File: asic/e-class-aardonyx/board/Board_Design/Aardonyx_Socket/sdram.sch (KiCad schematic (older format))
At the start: 30 parts, among them J4 Conn_1x4, U15 SKT32E, U2 IS42S32160F-TSOP2, U3 CDCE913PW, Y2 27MHz

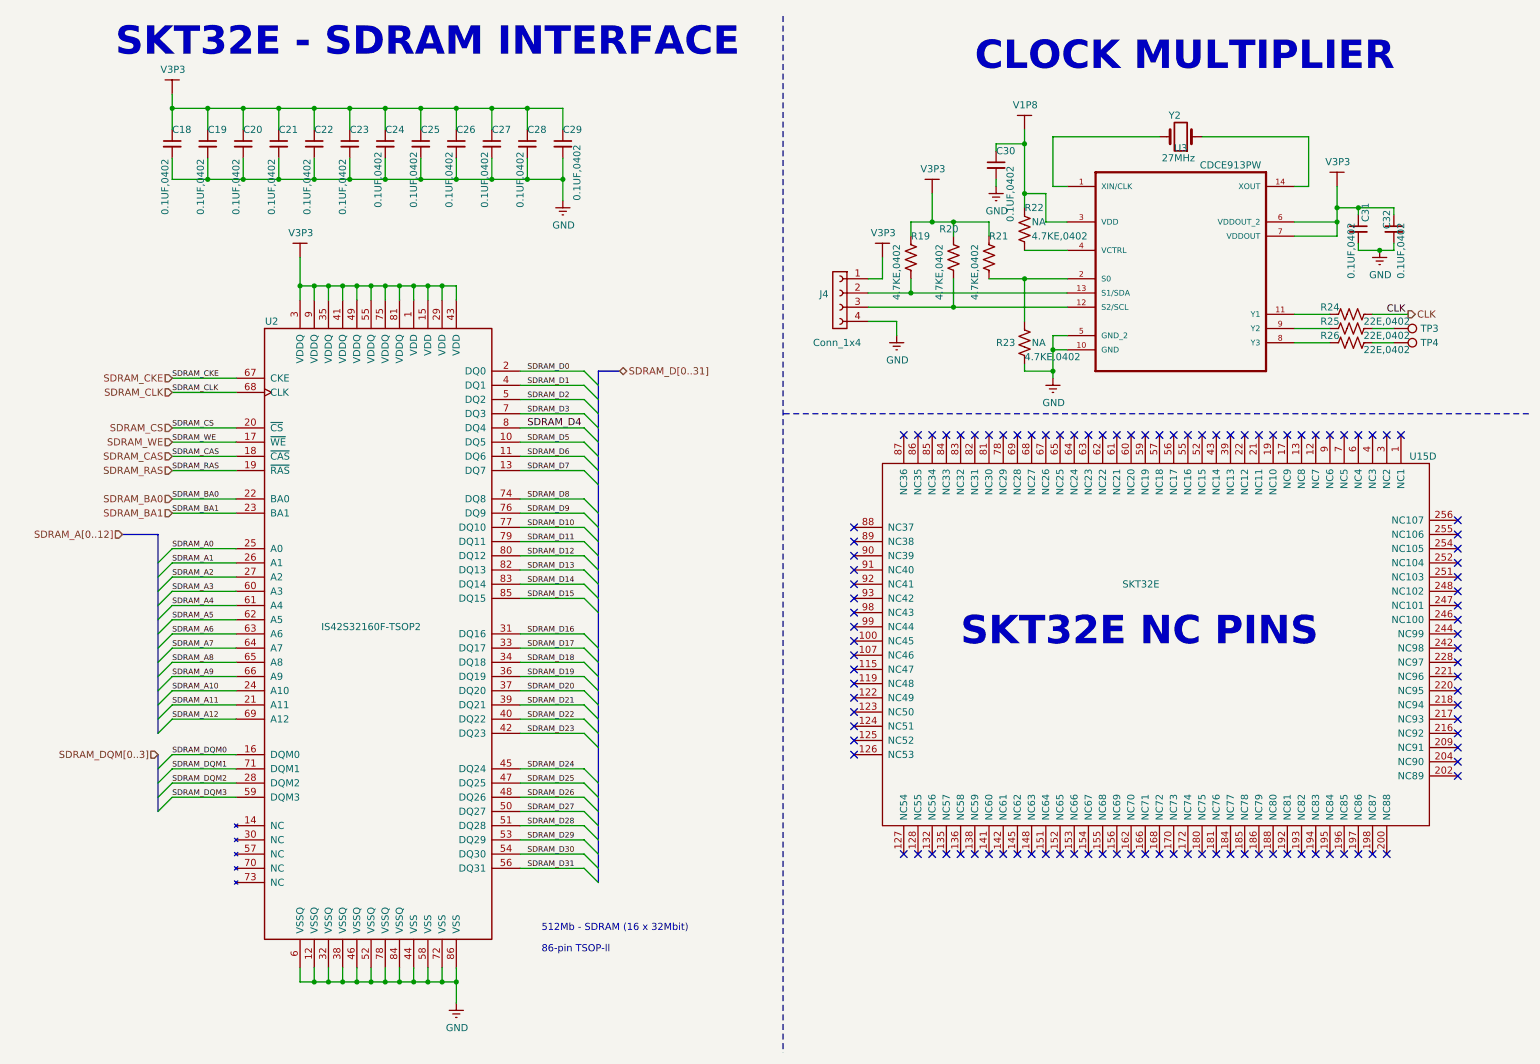
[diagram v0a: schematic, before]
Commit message: update socket compo placement
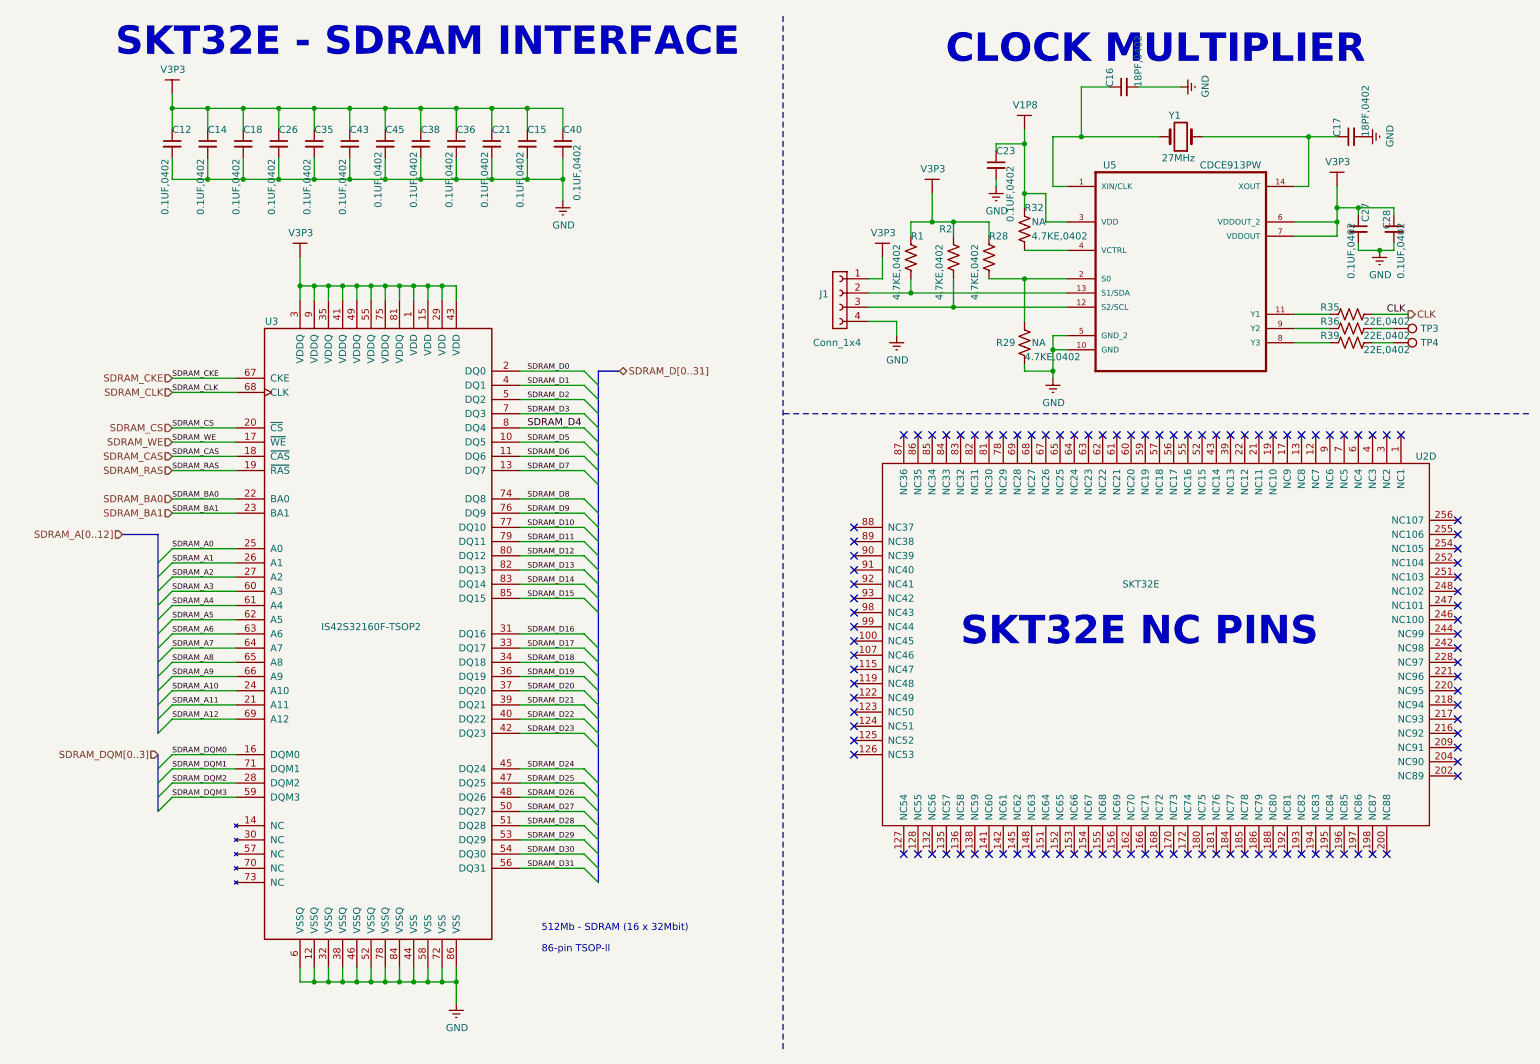
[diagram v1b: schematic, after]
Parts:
- added C16, C17: 18PF,0402, Capacitor_SMD:C_0402_1005Metric, symbol Aardonyx-rescue:C_Small-aardonyx
- renumbered C18 to C12, C19 to C14, C28 to C15, C20 to C18, C27 to C21, C30 to C23, C21 to C26, C31 to C27, C32 to C28, C22 to C35, C26 to C36, C25 to C38, C29 to C40, C23 to C43, C24 to C45, J4 to J1, R19 to R1, R20 to R2, R21 to R28, R23 to R29, R22 to R32, R24 to R35, R25 to R36, R26 to R39, U15 to U2, U2 to U3, Y2 to Y1
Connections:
- net GNDREF: now also C16.2, C17.2
- net at U3.1 (XIN/CLK), Y1.2: now also C16.1
- net at U3.14 (XOUT), Y1.1: now also C17.1

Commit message: Back annotation
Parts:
- renumbered C16 to C17, C17 to C18, C23 to C26, C27 to C29, C28 to C30, C38 to C35, C26 to C38, C12 to C39, C14 to C42, C36 to C43, C35 to C44, C21 to C47, C40 to C48, C15 to C50, C43 to C51, C18 to C52, J1 to J6, R28 to R45, R29 to R46, R32 to R49, R35 to R50, R36 to R52, R39 to R57, R1 to R68, R2 to R69, U2 to U1, U3 to U7
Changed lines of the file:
@@
 $EndDescr
 $Comp
-L Aardonyx-rescue:IS42S32160F-TSOP2-aardonyx U3
+L Aardonyx-rescue:IS42S32160F-TSOP2-aardonyx U7
 U 1 1 5DB67858
 P 3100 4800
-F 0 "U3" H 2350 6950 50  0000 C CNN
+F 0 "U7" H 2350 6950 50  0000 C CNN
 F 1 "IS42S32160F-TSOP2" H 3050 4800 50  0000 C CNN
 F 2 "Aardonyx:TSSOP-II-86_10.16x22.2mm_P0.5mm" H 3100 4950 50  0001 C CNN
@@
 	1650 3150 2100 3150
 $Comp
-L Aardonyx-rescue:C_Small-aardonyx C12
+L Aardonyx-rescue:C_Small-aardonyx C39
 U 1 1 5DBB071C
 P 1650 1400
-F 0 "C12" H 1650 1500 50  0000 L CNN
+F 0 "C39" H 1650 1500 50  0000 L CNN
 F 1 "0.1UF,0402" V 1600 900 50  0000 L CNN
 F 2 "Capacitor_SMD:C_0402_1005Metric" H 1650 1400 50  0001 C CNN
@@
 $EndComp
 $Comp
-L Aardonyx-rescue:C_Small-aardonyx C14
+L Aardonyx-rescue:C_Small-aardonyx C42
 U 1 1 5DBD6F2F
 P 1900 1400
-F 0 "C14" H 1900 1500 50  0000 L CNN
+F 0 "C42" H 1900 1500 50  0000 L CNN
 F 1 "0.1UF,0402" V 1850 900 50  0000 L CNN
 F 2 "Capacitor_SMD:C_0402_1005Metric" H 1900 1400 50  0001 C CNN
@@
 $EndComp
 $Comp
-L Aardonyx-rescue:C_Small-aardonyx C18
+L Aardonyx-rescue:C_Small-aardonyx C52
 U 1 1 5DBDAFB5
 P 2150 1400
-F 0 "C18" H 2150 1500 50  0000 L CNN
+F 0 "C52" H 2150 1500 50  0000 L CNN
 F 1 "0.1UF,0402" V 2100 900 50  0000 L CNN
 F 2 "Capacitor_SMD:C_0402_1005Metric" H 2150 1400 50  0001 C CNN
@@
 $EndComp
 $Comp
-L Aardonyx-rescue:C_Small-aardonyx C26
+L Aardonyx-rescue:C_Small-aardonyx C38
 U 1 1 5DBE0332
 P 2400 1400
-F 0 "C26" H 2400 1500 50  0000 L CNN
+F 0 "C38" H 2400 1500 50  0000 L CNN
 F 1 "0.1UF,0402" V 2350 900 50  0000 L CNN
 F 2 "Capacitor_SMD:C_0402_1005Metric" H 2400 1400 50  0001 C CNN
@@
 $EndComp
 $Comp
-L Aardonyx-rescue:C_Small-aardonyx C35
+L Aardonyx-rescue:C_Small-aardonyx C44
 U 1 1 5DBE0338
 P 2650 1400
-F 0 "C35" H 2650 1500 50  0000 L CNN
+F 0 "C44" H 2650 1500 50  0000 L CNN
 F 1 "0.1UF,0402" V 2600 900 50  0000 L CNN
 F 2 "Capacitor_SMD:C_0402_1005Metric" H 2650 1400 50  0001 C CNN
@@
 $EndComp
 $Comp
-L Aardonyx-rescue:C_Small-aardonyx C43
+L Aardonyx-rescue:C_Small-aardonyx C51
 U 1 1 5DBE033E
 P 2900 1400
-F 0 "C43" H 2900 1500 50  0000 L CNN
+F 0 "C51" H 2900 1500 50  0000 L CNN
 F 1 "0.1UF,0402" V 2850 900 50  0000 L CNN
 F 2 "Capacitor_SMD:C_0402_1005Metric" H 2900 1400 50  0001 C CNN
@@
 $EndComp
 $Comp
-L Aardonyx-rescue:C_Small-aardonyx C38
+L Aardonyx-rescue:C_Small-aardonyx C35
 U 1 1 5DBE55F5
 P 3400 1400
-F 0 "C38" H 3400 1500 50  0000 L CNN
+F 0 "C35" H 3400 1500 50  0000 L CNN
 F 1 "0.1UF,0402" V 3350 950 50  0000 L CNN
 F 2 "Capacitor_SMD:C_0402_1005Metric" H 3400 1400 50  0001 C CNN
@@
 $EndComp
 $Comp
-L Aardonyx-rescue:C_Small-aardonyx C36
+L Aardonyx-rescue:C_Small-aardonyx C43
 U 1 1 5DBE55FB
 P 3650 1400
-F 0 "C36" H 3650 1500 50  0000 L CNN
+F 0 "C43" H 3650 1500 50  0000 L CNN
 F 1 "0.1UF,0402" V 3600 950 50  0000 L CNN
 F 2 "Capacitor_SMD:C_0402_1005Metric" H 3650 1400 50  0001 C CNN
@@
 $EndComp
 $Comp
-L Aardonyx-rescue:C_Small-aardonyx C21
+L Aardonyx-rescue:C_Small-aardonyx C47
 U 1 1 5DBE5601
 P 3900 1400
-F 0 "C21" H 3900 1500 50  0000 L CNN
+F 0 "C47" H 3900 1500 50  0000 L CNN
 F 1 "0.1UF,0402" V 3850 950 50  0000 L CNN
 F 2 "Capacitor_SMD:C_0402_1005Metric" H 3900 1400 50  0001 C CNN
@@
 $EndComp
 $Comp
-L Aardonyx-rescue:C_Small-aardonyx C15
+L Aardonyx-rescue:C_Small-aardonyx C50
 U 1 1 5DBE5607
 P 4150 1400
-F 0 "C15" H 4150 1500 50  0000 L CNN
+F 0 "C50" H 4150 1500 50  0000 L CNN
 F 1 "0.1UF,0402" V 4100 950 50  0000 L CNN
 F 2 "Capacitor_SMD:C_0402_1005Metric" H 4150 1400 50  0001 C CNN
@@
 $EndComp
 $Comp
-L Aardonyx-rescue:C_Small-aardonyx C40
+L Aardonyx-rescue:C_Small-aardonyx C48
 U 1 1 5DBE560D
 P 4400 1400
-F 0 "C40" H 4400 1500 50  0000 L CNN
+F 0 "C48" H 4400 1500 50  0000 L CNN
 F 1 "0.1UF,0402" V 4500 1000 50  0000 L CNN
 F 2 "Capacitor_SMD:C_0402_1005Metric" H 4400 1400 50  0001 C CNN
@@
 P 7150 2200
 AR Path="/5D8B3740/5EFB4D01" Ref="R?"  Part="1"
-AR Path="/5D8B37B8/5EFB4D01" Ref="R2"  Part="1"
-F 0 "R2" H 7050 2400 50  0000 L CNN
+AR Path="/5D8B37B8/5EFB4D01" Ref="R69"  Part="1"
+F 0 "R69" H 7050 2400 50  0000 L CNN
 F 1 "4.7KE,0402" V 7050 1900 50  0000 L CNN
 F 2 "Resistor_SMD:R_0402_1005Metric" V 7190 2190 50  0001 C CNN
@@
 P 6850 2200
 AR Path="/5D8B3740/5EFB4D07" Ref="R?"  Part="1"
-AR Path="/5D8B37B8/5EFB4D07" Ref="R1"  Part="1"
-F 0 "R1" H 6850 2350 50  0000 L CNN
+AR Path="/5D8B37B8/5EFB4D07" Ref="R68"  Part="1"
+F 0 "R68" H 6850 2350 50  0000 L CNN
 F 1 "4.7KE,0402" V 6750 1900 50  0000 L CNN
 F 2 "Resistor_SMD:R_0402_1005Metric" V 6890 2190 50  0001 C CNN
@@
 P 10000 2000
 AR Path="/5D8B3740/5EFB4D13" Ref="C?"  Part="1"
-AR Path="/5D8B37B8/5EFB4D13" Ref="C27"  Part="1"
-F 0 "C27" V 10050 2050 50  0000 L CNN
+AR Path="/5D8B37B8/5EFB4D13" Ref="C29"  Part="1"
+F 0 "C29" V 10050 2050 50  0000 L CNN
 F 1 "0.1UF,0402" V 9950 1650 50  0000 L CNN
 F 2 "Capacitor_SMD:C_0402_1005Metric" H 10000 2000 50  0001 C CNN
@@
 P 10250 2000
 AR Path="/5D8B3740/5EFB4D19" Ref="C?"  Part="1"
-AR Path="/5D8B37B8/5EFB4D19" Ref="C28"  Part="1"
-F 0 "C28" V 10200 2000 50  0000 L CNN
+AR Path="/5D8B37B8/5EFB4D19" Ref="C30"  Part="1"
+F 0 "C30" V 10200 2000 50  0000 L CNN
 F 1 "0.1UF,0402" V 10300 1650 50  0000 L CNN
 F 2 "Capacitor_SMD:C_0402_1005Metric" H 10250 2000 50  0001 C CNN
@@
 P 9950 2600
 AR Path="/5D8B3740/5EFB4D80" Ref="R?"  Part="1"
-AR Path="/5D8B37B8/5EFB4D80" Ref="R35"  Part="1"
-F 0 "R35" V 9900 2450 50  0000 C CNN
+AR Path="/5D8B37B8/5EFB4D80" Ref="R50"  Part="1"
+F 0 "R50" V 9900 2450 50  0000 C CNN
 F 1 "22E,0402" V 10000 2850 50  0000 C CNN
 F 2 "Resistor_SMD:R_0402_1005Metric" V 9990 2590 50  0001 C CNN
@@
 P 7400 2200
 AR Path="/5D8B3740/5F80E136" Ref="R?"  Part="1"
-AR Path="/5D8B37B8/5F80E136" Ref="R28"  Part="1"
-F 0 "R28" H 7400 2350 50  0000 L CNN
+AR Path="/5D8B37B8/5F80E136" Ref="R45"  Part="1"
+F 0 "R45" H 7400 2350 50  0000 L CNN
 F 1 "4.7KE,0402" V 7300 1900 50  0000 L CNN
 F 2 "Resistor_SMD:R_0402_1005Metric" V 7440 2190 50  0001 C CNN
@@
 P 7650 2800
 AR Path="/5D8B3740/5F82D0FE" Ref="R?"  Part="1"
-AR Path="/5D8B37B8/5F82D0FE" Ref="R29"  Part="1"
-F 0 "R29" H 7450 2800 50  0000 L CNN
+AR Path="/5D8B37B8/5F82D0FE" Ref="R46"  Part="1"
+F 0 "R46" H 7450 2800 50  0000 L CNN
 F 1 "4.7KE,0402" H 7650 2700 50  0000 L CNN
 F 2 "Resistor_SMD:R_0402_1005Metric" V 7690 2790 50  0001 C CNN
@@
 P 7650 2000
 AR Path="/5D8B3740/5F8A4363" Ref="R?"  Part="1"
-AR Path="/5D8B37B8/5F8A4363" Ref="R32"  Part="1"
-F 0 "R32" H 7650 2150 50  0000 L CNN
+AR Path="/5D8B37B8/5F8A4363" Ref="R49"  Part="1"
+F 0 "R49" H 7650 2150 50  0000 L CNN
 F 1 "4.7KE,0402" H 7700 1950 50  0000 L CNN
 F 2 "Resistor_SMD:R_0402_1005Metric" V 7690 1990 50  0001 C CNN
@@
 P 7450 1550
 AR Path="/5D8B3740/5F8E5F7E" Ref="C?"  Part="1"
-AR Path="/5D8B37B8/5F8E5F7E" Ref="C23"  Part="1"
-F 0 "C23" H 7450 1650 50  0000 L CNN
+AR Path="/5D8B37B8/5F8E5F7E" Ref="C26"  Part="1"
+F 0 "C26" H 7450 1650 50  0000 L CNN
 F 1 "0.1UF,0402" V 7550 1150 50  0000 L CNN
 F 2 "Capacitor_SMD:C_0402_1005Metric" H 7450 1550 50  0001 C CNN
@@
 SDRAM_BA0
 $Comp
-L Aardonyx-rescue:Conn_01x04-aardonyx J1
+L Aardonyx-rescue:Conn_01x04-aardonyx J6
 U 1 1 63AEA5D7
 P 6350 2450
-F 0 "J1" H 6430 2442 50  0000 L CNN
+F 0 "J6" H 6430 2442 50  0000 L CNN
 F 1 "Conn_1x4" H 6200 2100 50  0000 L CNN
 F 2 "Connector_PinHeader_2.54mm:PinHeader_1x04_P2.54mm_Vertical" H 6350 2450 50  0001 C CNN
@@
 P 9950 2800
 AR Path="/5D8B3740/5EF94816" Ref="R?"  Part="1"
-AR Path="/5D8B37B8/5EF94816" Ref="R39"  Part="1"
-F 0 "R39" V 9900 2650 50  0000 C CNN
+AR Path="/5D8B37B8/5EF94816" Ref="R57"  Part="1"
+F 0 "R57" V 9900 2650 50  0000 C CNN
 F 1 "22E,0402" V 10000 3050 50  0000 C CNN
 F 2 "Resistor_SMD:R_0402_1005Metric" V 9990 2790 50  0001 C CNN
@@
 P 9950 2700
 AR Path="/5D8B3740/5EF96060" Ref="R?"  Part="1"
-AR Path="/5D8B37B8/5EF96060" Ref="R36"  Part="1"
-F 0 "R36" V 9900 2550 50  0000 C CNN
+AR Path="/5D8B37B8/5EF96060" Ref="R52"  Part="1"
+F 0 "R52" V 9900 2550 50  0000 C CNN
 F 1 "22E,0402" V 10000 2950 50  0000 C CNN
 F 2 "Resistor_SMD:R_0402_1005Metric" V 9990 2690 50  0001 C CNN
@@
 P 8750 2200
 AR Path="/5ED5EB9F" Ref="U3"  Part="1"
-AR Path="/5D8B37B8/5ED5EB9F" Ref="U5"  Part="1"
-F 0 "U5" H 8250 2850 50  0000 C CNN
+AR Path="/5D8B37B8/5ED5EB9F" Ref="U6"  Part="1"
+F 0 "U6" H 8250 2850 50  0000 C CNN
 F 1 "CDCE913PW" H 9100 2850 50  0000 C CNN
 F 2 "Package_SO:TSSOP-14_4.4x5mm_P0.65mm" H 8900 2000 50  0001 L BNN
@@
 $EndComp
 $Comp
-L Aardonyx-rescue:SKT32E-skt32e_asic U2
+L Aardonyx-rescue:SKT32E-skt32e_asic U1
 U 4 1 5ED60D0C
 P 9100 4500
-F 0 "U2" V 8200 5950 50  0000 R CNN
+F 0 "U1" V 8200 5950 50  0000 R CNN
 F 1 "SKT32E" V 9100 4000 50  0000 R CNN
 F 2 "Aardonyx:SKT32E_IITM_TH_SOCKET" H 8250 5900 50  0001 C CNN
@@
 Connection ~ 7650 1400
 $Comp
-L Aardonyx-rescue:C_Small-aardonyx C17
+L Aardonyx-rescue:C_Small-aardonyx C18
 U 1 1 5F202590
 P 9950 1350
-F 0 "C17" H 9950 1450 50  0000 L CNN
+F 0 "C18" H 9950 1450 50  0000 L CNN
 F 1 "18PF,0402" H 9950 1250 50  0000 L CNN
 F 2 "Capacitor_SMD:C_0402_1005Metric" H 9950 1350 50  0001 C CNN
@@
 $EndComp
 $Comp
-L Aardonyx-rescue:C_Small-aardonyx C16
+L Aardonyx-rescue:C_Small-aardonyx C17
 U 1 1 5F229012
 P 8350 1000
-F 0 "C16" H 8350 1100 50  0000 L CNN
+F 0 "C17" H 8350 1100 50  0000 L CNN
 F 1 "18PF,0402" H 8350 900 50  0000 L CNN
 F 2 "Capacitor_SMD:C_0402_1005Metric" H 8350 1000 50  0001 C CNN
